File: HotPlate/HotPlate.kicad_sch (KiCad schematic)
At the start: 61 parts, among them J1 USB_C_Receptacle_USB2.0_14P, J2 Heater, Q1 STU417S, Q4 MS50N06, SW1 RESET, SW2 BOOT, SW3 BTN0, SW4 BTN1, SW5 BTN2, SW6 BTN3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

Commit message: Change LED size
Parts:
- D1, D2: footprint Diode_SMD:D_0603_1608Metric -> Diode_SMD:D_1206_3216Metric
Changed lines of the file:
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@@
 			)
 		)
-		(property "Footprint" "Diode_SMD:D_0603_1608Metric"
+		(property "Footprint" "Diode_SMD:D_1206_3216Metric"
 			(at 165.1 119.38 0)
 			(hide yes)
@@
 			)
 		)
-		(property "Footprint" "Diode_SMD:D_0603_1608Metric"
+		(property "Footprint" "Diode_SMD:D_1206_3216Metric"
 			(at 165.1 128.27 0)
 			(hide yes)

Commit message: Change button footprint
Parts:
- SW1, SW2: footprint Button_Switch_SMD:SW_Push_1P1T_NO_CK_KMR2 -> Button_Switch_SMD:SW_SPST_PTS647_Sx38
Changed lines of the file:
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@@
 			)
 		)
-		(property "Footprint" "Button_Switch_SMD:SW_Push_1P1T_NO_CK_KMR2"
+		(property "Footprint" "Button_Switch_SMD:SW_SPST_PTS647_Sx38"
 			(at 60.96 175.26 0)
 			(hide yes)
@@
 			)
 		)
-		(property "Footprint" "Button_Switch_SMD:SW_Push_1P1T_NO_CK_KMR2"
+		(property "Footprint" "Button_Switch_SMD:SW_SPST_PTS647_Sx38"
 			(at 127 177.8 0)
 			(hide yes)

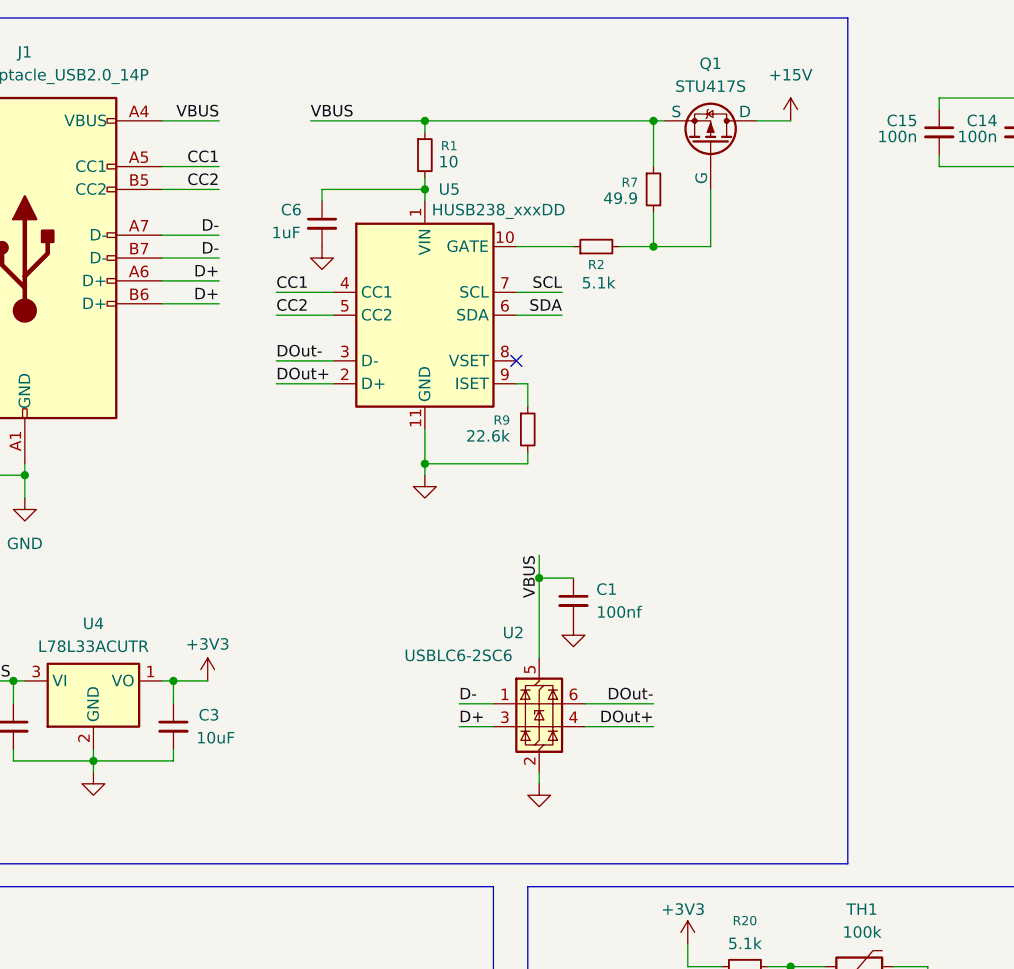
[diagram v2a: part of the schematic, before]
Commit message: Remove the USBLC6 since i forgot that im using 20v and not 5v
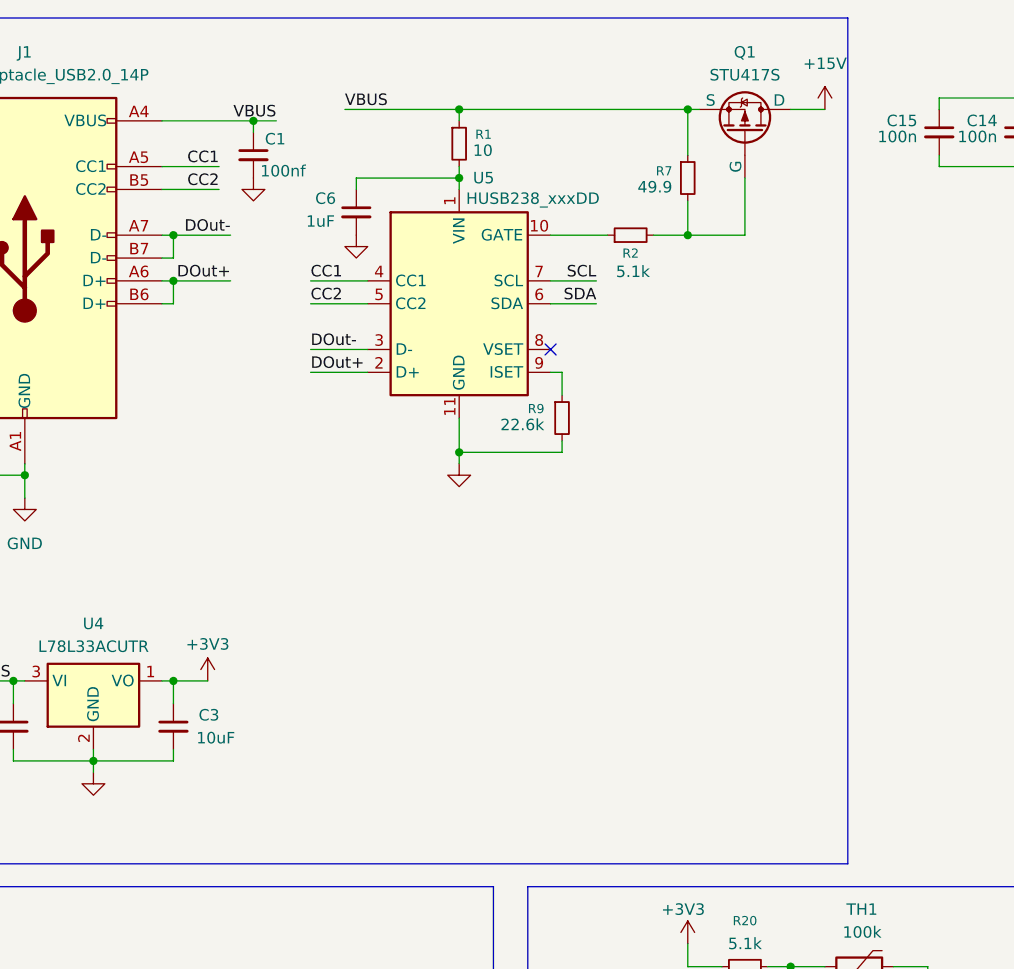
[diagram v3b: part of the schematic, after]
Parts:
- removed U2: USBLC6-2SC6, Package_TO_SOT_SMD:SOT-23-6, symbol Power_Protection:USBLC6-2SC6
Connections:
- net D+ is gone; now on net DOut+: J1.A6 (D+), J1.B6 (D+)
- net D- is gone; now on net DOut-: J1.A7 (D-), J1.B7 (D-)
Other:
- moved on the sheet: C1, C6, Q1, R1, R2, R7, R9, U5
